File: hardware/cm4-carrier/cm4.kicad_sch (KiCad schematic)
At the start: 4 parts, among them J3 Raspberry Pi CM4, J4 Raspberry Pi CM4

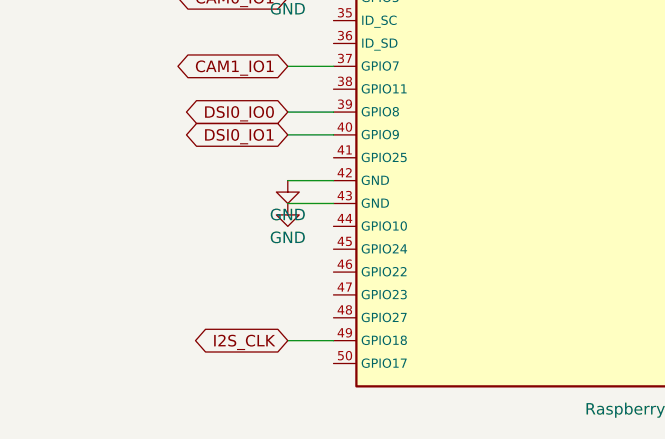
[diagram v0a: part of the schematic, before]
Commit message: Add volume up/down and sleep/wake push buttons
Add three user push buttons on the boot/control sheet:

- SW4 (volume up, GPIO22) and SW5 (volume down, GPIO23): momentary to GND with
  a 10k pull-up to 3.3V and a 100nF RC-debounce cap each; software reads them
  to adjust playback level.
- SW6 (sleep/wake) on GPIO3: with dtoverlay=gpio-shutdown a press cleanly halts
  the CM4 to save battery, and GPIO3 (the wake-from-halt pin) wakes it again.
  GPIO3 is also I2C1 SCL (already pulled up by the fuel gauge), so no debounce
  cap is used.

The CM4 sheet now exports GPIO22/GPIO23 as global nets VOL_UP/VOL_DN; the
sleep button ties to the existing SCL/GPIO3 net. README/BOM updated. No format
change (KiCad 10 schematic 20260306).

Co-Authored-By: Claude Opus 4.8 <noreply@anthropic.com>
Claude-Session: https://claude.ai/code/session_015B7X7FE461jFSRaiTFdnFt
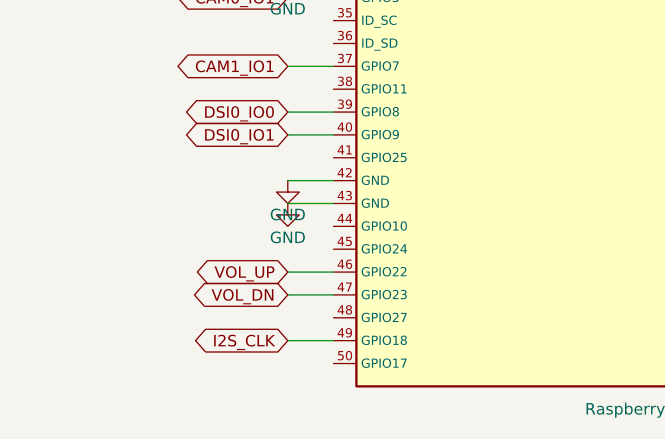
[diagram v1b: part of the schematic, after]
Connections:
- net VOL_UP: now reaches J3.46 (GPIO22)
- net VOL_DN: now reaches J3.47 (GPIO23)
